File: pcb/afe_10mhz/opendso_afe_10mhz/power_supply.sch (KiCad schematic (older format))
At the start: 21 parts, among them IC18 MCP1700T-2502E, IC19 MCP1700T-2502E, IC20 NCP718ASN500, IC21 XC6901D501ER-G

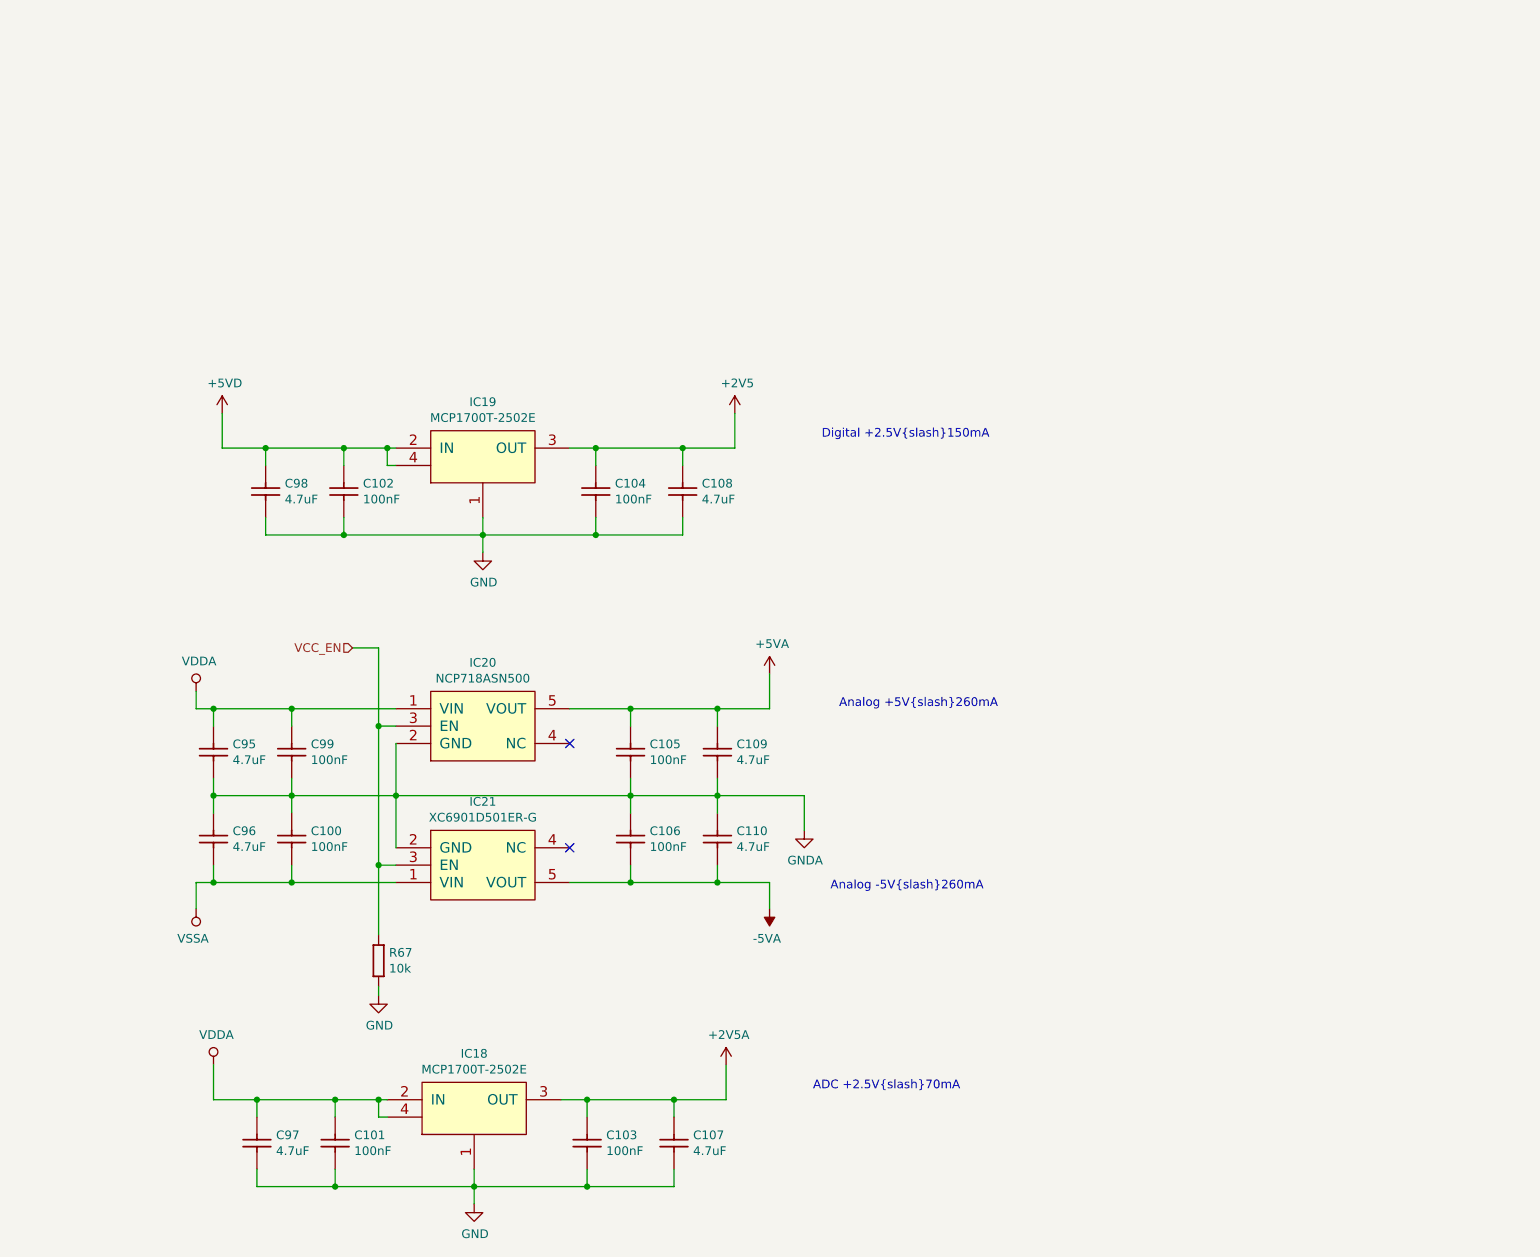
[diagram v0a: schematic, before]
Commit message: AFE schematic: finished port to KiCad
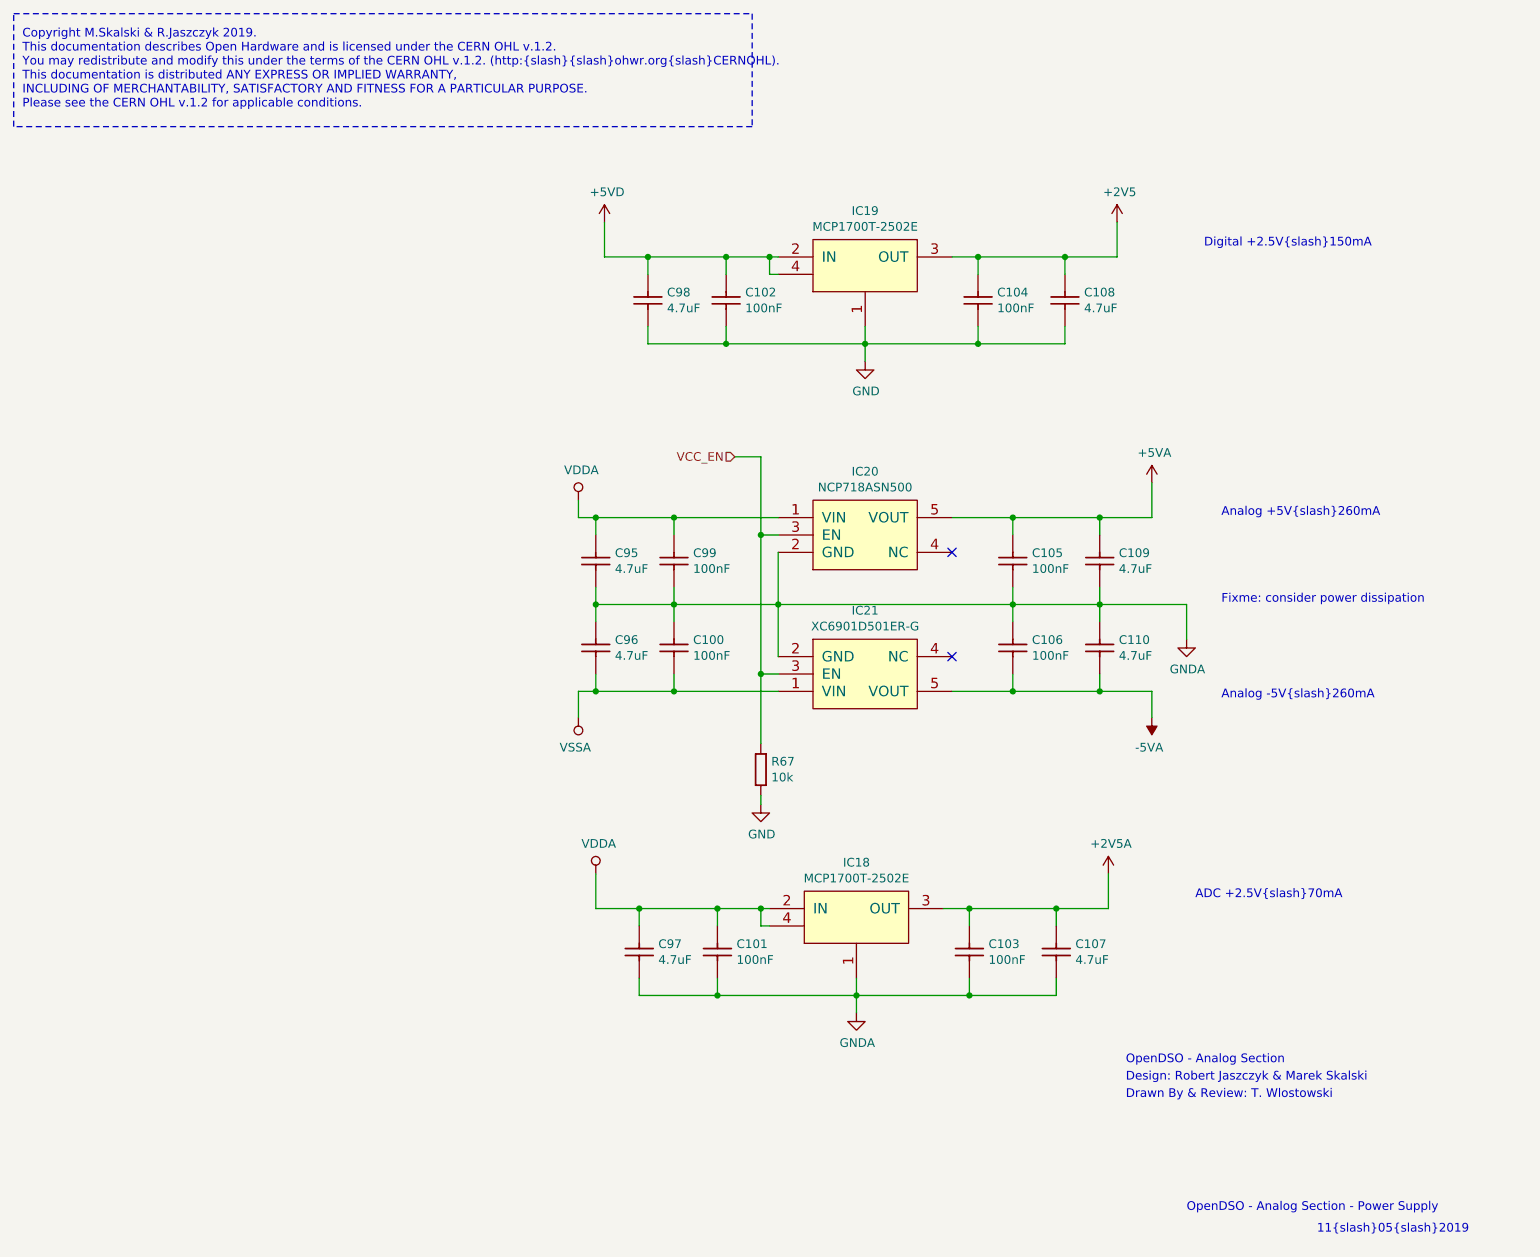
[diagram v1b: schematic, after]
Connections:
- net GND: no longer C101.1, C103.1, C107.1, C97.1, IC18.1 (GND)
- net GNDA: now also C101.1, C103.1, C107.1, C97.1, IC18.1 (GND)
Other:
- note added: "11/05/2019\n"
- note added: "Copyright M.Skalski & R.Jaszczyk 2019.\nThis documentation describes Open Hardware and is licensed under the CERN OHL v.1.2.\nYou may redistribute and modify this under the terms of the CERN OHL v.1.2. (http://ohwr.org/CERNOHL).\nThis documentation is distributed ANY EXPRESS OR IMPLIED WARRANTY,\nINCLUDING OF MERCHANTABILITY, SATISFACTORY AND FITNESS FOR A PARTICULAR PURPOSE.\nP…"
- note added: "Design: Robert Jaszczyk & Marek Skalski\n"
- note added: "Drawn By & Review: T. Wlostowski\n"
- note added: "Fixme: consider power dissipation"
- note added: "OpenDSO - Analog Section - Power Supply"
- note added: "OpenDSO - Analog Section\n"
- moved on the sheet: C100, C101, C102, C103, C104, C105, C106, C107, C108, C109, C110, C95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
